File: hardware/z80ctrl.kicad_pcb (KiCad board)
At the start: 2 copper layers, 100.1 x 49.9 mm, 25 parts, among them J1 BUS, J2 BUSEXT, J4 IOADDR, J5 SERIAL1, J6 SERIAL2, J7 SD, SW1 RESET, SW2 HALT, U1 74HCT139, U2 ATMEGA1284P-PU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

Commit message: Updated schematic
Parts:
- U1: footprint Housings_DIP:DIP-16_W7.62mm -> Housings_DIP:DIP-16_W7.62mm_Socket
- U2: footprint Housings_DIP:DIP-40_W15.24mm -> Housings_DIP:DIP-40_W15.24mm_Socket
- U3: footprint Housings_DIP:DIP-14_W7.62mm -> Housings_DIP:DIP-14_W7.62mm_Socket
- U4: footprint Housings_DIP:DIP-28_W7.62mm -> Housings_DIP:DIP-28_W7.62mm_Socket
- moved C4 19.2 mm to (217.7, 125.0)
- moved C6 13.7 mm to (201.4, 105.7), turned to 270 degrees
- moved C7 11.8 mm to (173.5, 127.5)
- moved SW2 9.16 mm to (251.5, 111.5), turned to 180 degrees
- moved U3 2.54 mm to (215.1, 106.9)
- moved C1 0.51 mm to (181.1, 146.3)
- moved C5 0.51 mm to (229.4, 125.5)
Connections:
- U2 pad 18: /WR -> /IOACK
- U2 pad 19: /RD -> /IORQ2
- U2 pad 21: /IOACK -> /M1
- U2 pad 3: /IORQ2 -> Net-(D1-Pad2)
- U2 pad 4: Net-(D1-Pad2) -> /RD
- U2 pad 5: IOXINT -> /WR
- U4 pad 2: /M1 -> /RFSH
- U4 pad 20: IOXINT -> Net-(U4-Pad20)
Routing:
- net IOXINT: track 64.6 -> 0.00 mm
- net /M1: track 58.7 -> 8.67 mm, vias 2 -> 0
- net /RFSH: track 0.00 -> 48.7 mm, vias 0 -> 1
- net A7: track 143.7 -> 97.5 mm, vias 1 -> 2
- net GND: track 225.8 -> 257.5 mm, vias 1 -> 4
- net /IOXCS: track 90.4 -> 118.7 mm
- net /WR: track 25.1 -> 51.2 mm, vias 0 -> 1
- net /IORQ2: track 69.5 -> 47.7 mm, vias 0 -> 1
- net /RD: track 30.1 -> 50.7 mm
- net A6: track 121.2 -> 101.1 mm, vias 0 -> 2
- net /WAIT: track 48.8 -> 31.1 mm, vias 2 -> 0
- net /HALT: track 82.3 -> 67.2 mm
- net A0: track 64.3 -> 78.1 mm, vias 0 -> 1
- net /IOACK: track 39.9 -> 26.5 mm, vias 1 -> 0
- net Net-(C7-Pad1): track 35.2 -> 22.0 mm, vias 1 -> 0
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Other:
- board size 100.1 x 49.9 mm -> 100 x 49.9 mm

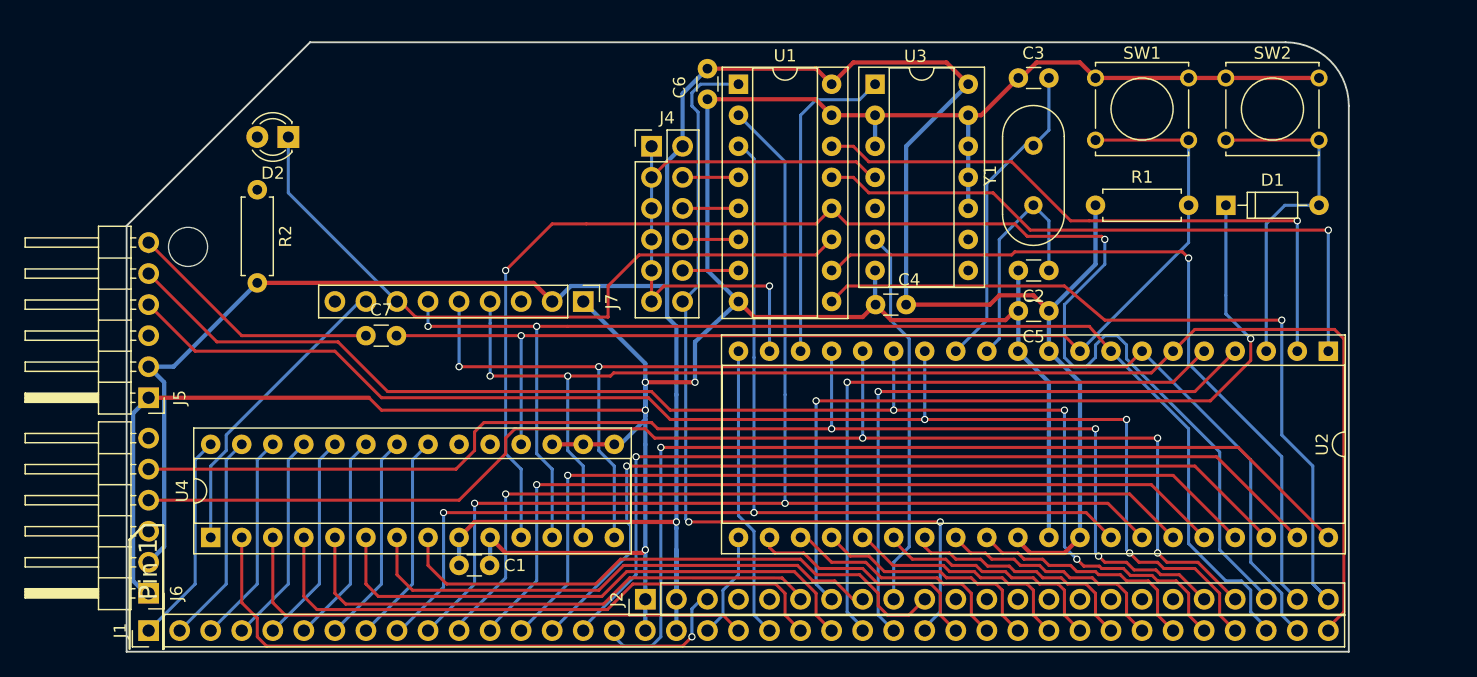
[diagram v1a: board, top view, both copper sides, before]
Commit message: Reroute to reduce via count
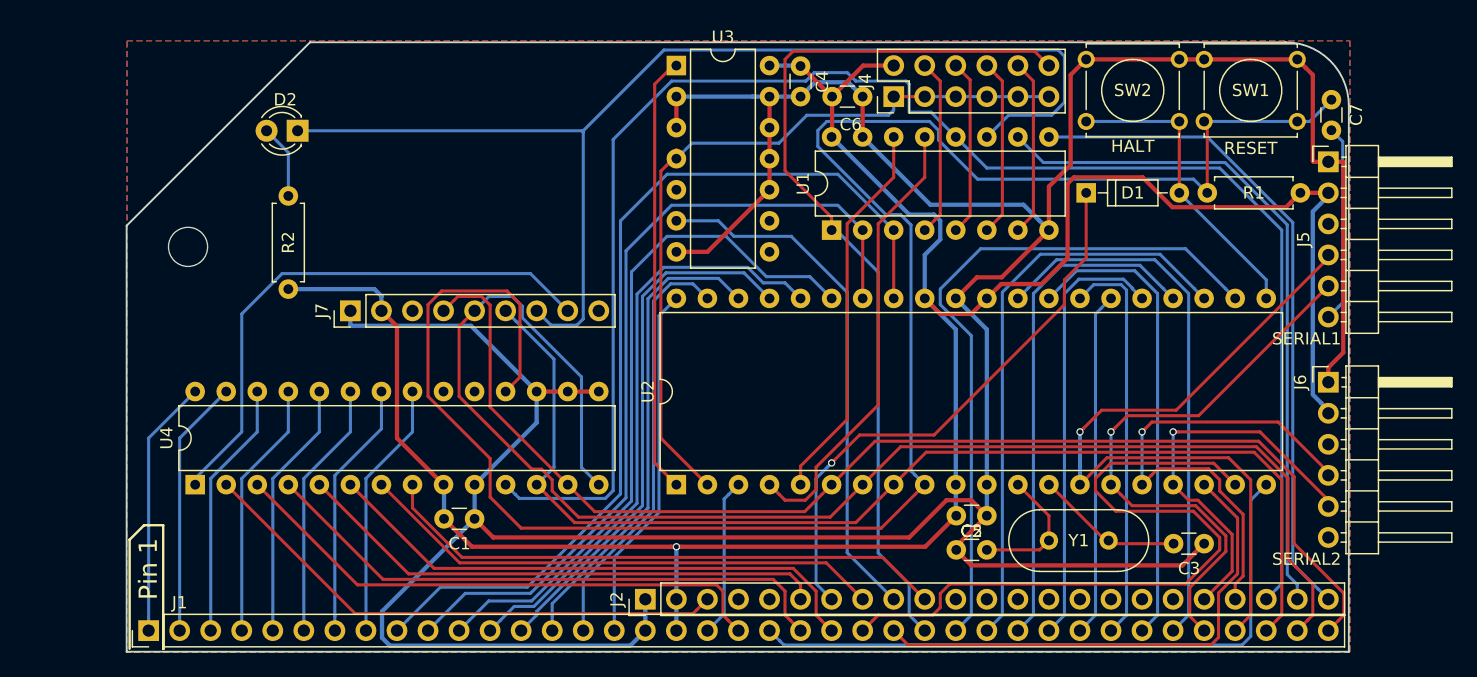
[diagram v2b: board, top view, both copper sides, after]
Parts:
- U1: footprint Housings_DIP:DIP-16_W7.62mm_Socket -> Housings_DIP:DIP-16_W7.62mm
- U2: footprint Housings_DIP:DIP-40_W15.24mm_Socket -> Housings_DIP:DIP-40_W15.24mm
- U3: footprint Housings_DIP:DIP-14_W7.62mm_Socket -> Housings_DIP:DIP-14_W7.62mm
- U4: footprint Housings_DIP:DIP-28_W7.62mm_Socket -> Housings_DIP:DIP-28_W7.62mm
- moved J5 98.4 mm to (252.2, 113.3), turned to 0 degrees
- moved J6 98.1 mm to (252.2, 131.3), turned to 0 degrees
- moved C7 80.8 mm to (252.5, 110.7), turned to 90 degrees
- moved U2 54.4 mm to (198.9, 139.7), turned to 90 degrees
- moved C3 39.4 mm to (239.6, 144.5), turned to 0 degrees
- moved Y1 27.5 mm to (229.4, 144.3), turned to 0 degrees
- moved C2 23.4 mm to (224.3, 145.0)
- moved C4 21.3 mm to (209.0, 105.5), turned to 270 degrees
- moved J4 20.2 mm to (216.7, 108.0), turned to 90 degrees
- moved J7 19.1 mm to (172.2, 125.5), turned to 90 degrees
- moved C5 18.4 mm to (221.8, 142.2), turned to 0 degrees
- moved R1 16.8 mm to (249.9, 115.8), turned to 180 degrees
- moved U3 16.3 mm to (198.9, 105.4)
- moved U1 14.2 mm to (211.6, 118.9), turned to 90 degrees
- moved SW2 11.5 mm to (240.0, 110.0)
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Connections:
- U2 pad 1: SPIA0 -> /IOACK
- U2 pad 18: /IOACK -> /RD
- U2 pad 19: /IORQ2 -> /WR
- U2 pad 2: SPIA1 -> /IORQ2
- U2 pad 21: /M1 -> Net-(D1-Pad2)
- U2 pad 3: Net-(D1-Pad2) -> /M1
- U2 pad 4: /RD -> SPIA0
- U2 pad 5: /WR -> SPIA1
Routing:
- net TX2: track 107.6 -> 32.5 mm, vias 3 -> 1
- net RX2: track 110.7 -> 40.1 mm, vias 3 -> 1
- net /AVRRST: track 93.9 -> 157.5 mm, vias 1 -> 0
- net TX: track 110.9 -> 47.6 mm, vias 3 -> 1
- net RX: track 112.8 -> 63.2 mm, vias 3 -> 1
- net A0: track 78.1 -> 29.3 mm, vias 1 -> 0
- net /SDCS: track 57.3 -> 96.9 mm
- net A1: track 72.9 -> 34.8 mm, vias 1 -> 0
- net D0: track 19.9 -> 56.7 mm
- net GND: track 257.5 -> 293.3 mm, vias 4 -> 0
- net VCC: track 227.8 -> 194.9 mm
- net A6: track 101.1 -> 68.2 mm, vias 2 -> 0
- net A2: track 71.0 -> 39.2 mm, vias 1 -> 0
- net CLK: track 23.9 -> 53.1 mm
- net D1: track 19.4 -> 47.5 mm
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- added copper zone on B.Cu, net GND
- added copper zone on F.Cu, net GND

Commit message: Add jumpers to disconnect VCC net from serial connector
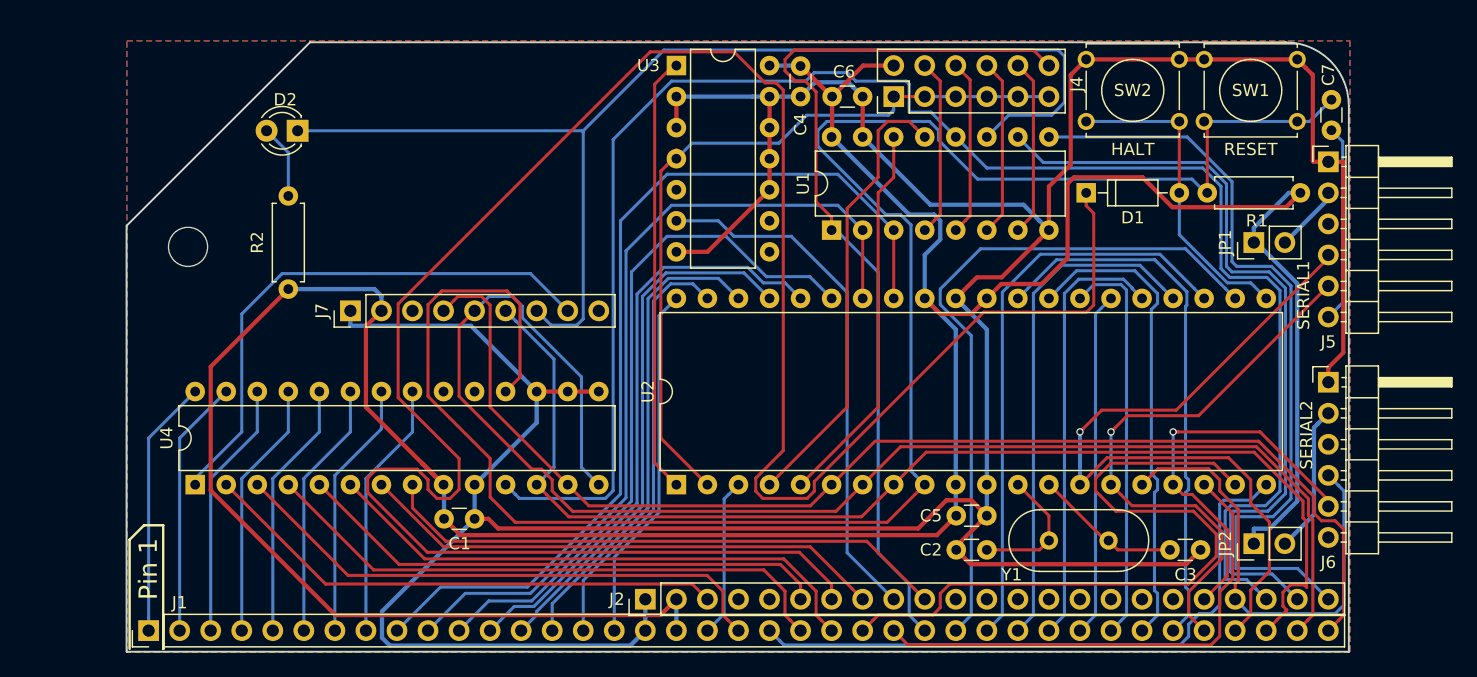
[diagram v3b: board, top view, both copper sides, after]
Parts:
- added JP1: Jumper, Pin_Headers:Pin_Header_Straight_1x02_Pitch2.54mm, F.Cu at (246.1, 119.9)
- added JP2: Jumper, Pin_Headers:Pin_Header_Straight_1x02_Pitch2.54mm, F.Cu at (246.1, 144.5)
- moved C3 0.59 mm to (239.3, 145.0)
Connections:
- J5 pad 2: VCC -> Net-(J5-Pad2)
- J6 pad 2: VCC -> Net-(J6-Pad2)
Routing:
- net /HALT: track 46.6 -> 189.7 mm, vias 1 -> 0
- net VCC: track 194.9 -> 268.2 mm, vias 1 -> 0
- net Net-(J6-Pad2): track 0.00 -> 12.1 mm
- net /AUXCS2: track 54.9 -> 64.0 mm
- net /AUXCS1: track 56.0 -> 64.1 mm
- net /IOXCS: track 132.6 -> 138.9 mm
- net Net-(J5-Pad2): track 0.00 -> 5.54 mm
- net SCK: track 94.9 -> 97.5 mm
- net RX2: track 40.1 -> 38.6 mm, vias 1 -> 0
- net RX: track 63.2 -> 64.5 mm
- net GND: track 293.3 -> 292.1 mm
- net CLK: track 53.1 -> 52.0 mm
- net Net-(D1-Pad2): track 25.0 -> 26.2 mm
- net /RFSH: track 44.2 -> 43.3 mm
- net D6: track 38.7 -> 39.3 mm
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
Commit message: Tweak routes
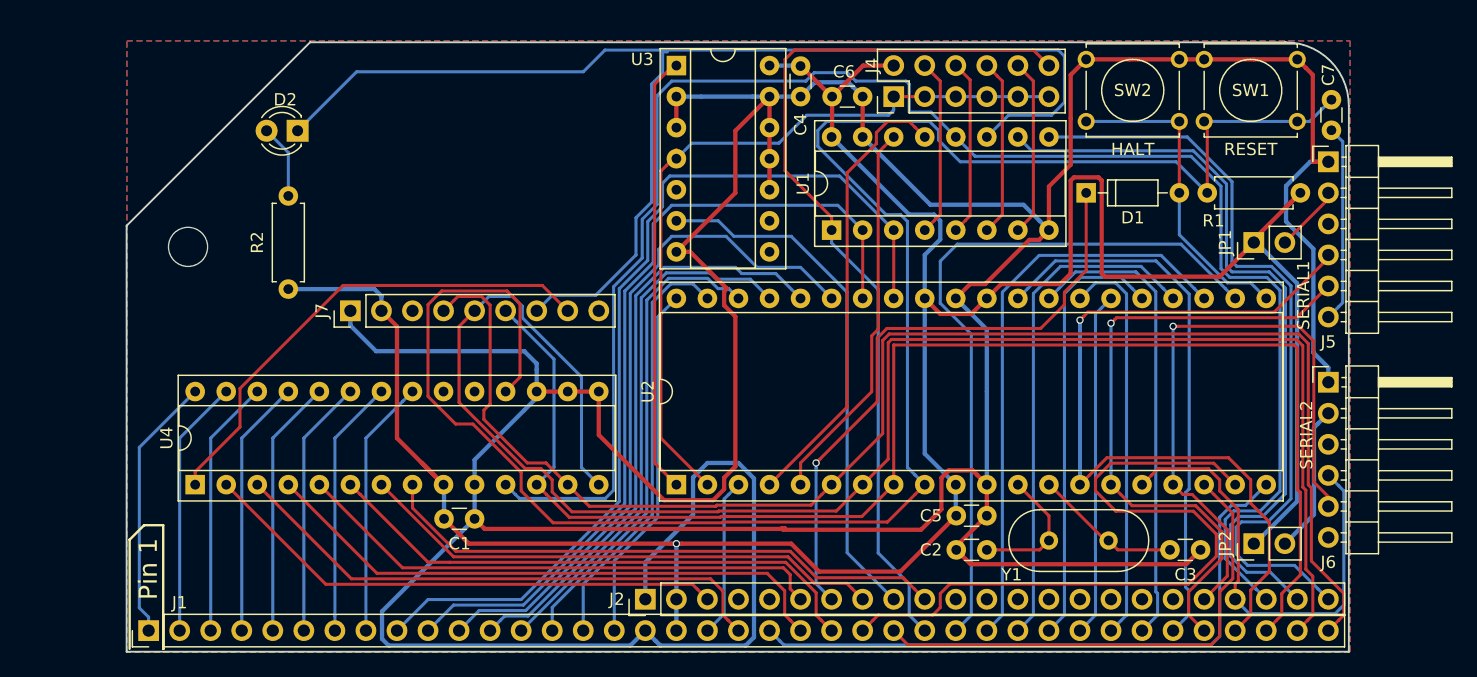
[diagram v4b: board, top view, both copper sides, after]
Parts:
- U1: footprint Housings_DIP:DIP-16_W7.62mm -> Housings_DIP:DIP-16_W7.62mm_Socket
- U2: footprint Housings_DIP:DIP-40_W15.24mm -> Housings_DIP:DIP-40_W15.24mm_Socket
- U3: footprint Housings_DIP:DIP-14_W7.62mm -> Housings_DIP:DIP-14_W7.62mm_Socket
- U4: footprint Housings_DIP:DIP-28_W7.62mm -> Housings_DIP:DIP-28_W7.62mm_Socket
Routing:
- net /HALT: track 189.7 -> 50.3 mm, vias 0 -> 1
- net GND: track 292.1 -> 381.3 mm
- net VCC: track 268.2 -> 217.1 mm, vias 0 -> 1
- net MISO: track 118.8 -> 139.1 mm
- net MOSI: track 100.9 -> 120.4 mm
- net SCK: track 97.5 -> 116.8 mm
- net TX2: track 32.1 -> 51.3 mm
- net RX: track 64.5 -> 79.0 mm
- net /SDCS: track 96.9 -> 105.0 mm
- net TX: track 47.4 -> 52.6 mm
- net /SDCD: track 44.8 -> 41.1 mm
- net D0: track 56.7 -> 58.3 mm
- net /IOXCS: track 138.9 -> 137.5 mm
- net /AUXCS1: track 64.1 -> 62.8 mm
- net /AUXCS2: track 64.0 -> 62.8 mm
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
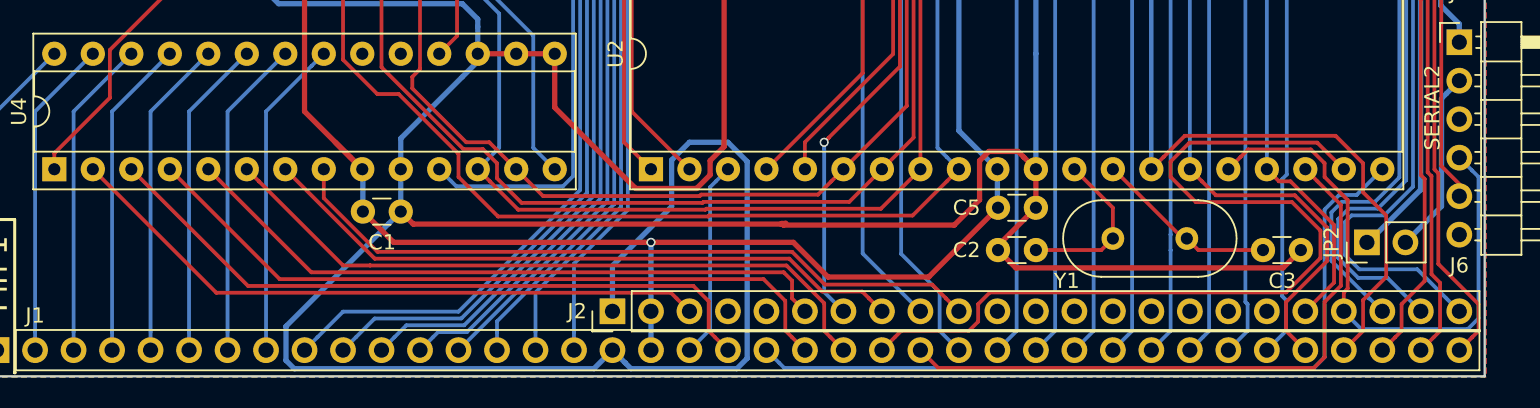
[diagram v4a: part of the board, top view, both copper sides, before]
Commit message: Add diode to prevent reset button from short circuiting
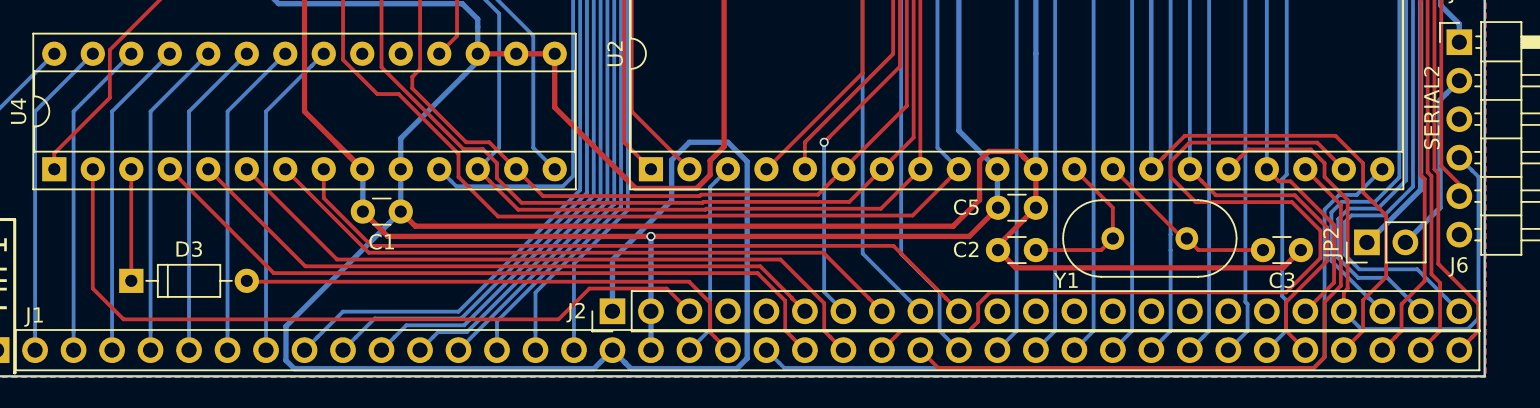
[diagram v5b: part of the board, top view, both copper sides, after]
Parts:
- added D3: 1N4148, Diodes_THT:D_DO-35_SOD27_P7.62mm_Horizontal, F.Cu at (164.6, 147.1)
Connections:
- net CLK2 renamed Net-(J2-Pad5)
- net PAGE renamed Net-(J2-Pad4)
- U4 pad 3: /RST -> Net-(D3-Pad1)
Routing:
- net /RST: track 45.5 -> 34.5 mm
- net Net-(D3-Pad1): track 0.00 -> 7.11 mm
- net /RFSH: track 43.3 -> 49.5 mm
- net VCC: track 217.1 -> 215.3 mm
- net /BUSACK: track 43.9 -> 43.3 mm

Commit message: Final tweaks before submitting REV1
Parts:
- moved C3 0.25 mm to (239.5, 145.0)
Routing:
- net /SDCD: track 41.1 -> 46.4 mm
- net SPIA0: track 37.3 -> 38.9 mm
- net /RFSH: track 49.5 -> 48.5 mm
- net /SDCS: track 105.0 -> 104.2 mm
- net Net-(J5-Pad2): track 6.04 -> 6.55 mm
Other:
- board size 100 x 49.9 mm -> 99.8 x 49.9 mm
- board text added: "(C)2018 J.B. Langston https://github.com/jblang/z80ctrl"
- board text added: "J4: IO addresses - None (left) - 00-3F - 40-7F - 80-BF - C0-FF - 00-FF (right) JP1: VCC from SERIAL1 JP2: VCC from SERIAL2"
- board text added: "microSD Pololu sdc02a"
